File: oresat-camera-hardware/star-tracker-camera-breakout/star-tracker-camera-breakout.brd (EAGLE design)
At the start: 31.8 x 86.4 mm, 7 parts, among them J1 3-1734592-64-1734592-0, J2 3-1734592-64-1734592-0, J7 2X6 FEMALE, J8 2X6 FEMALE

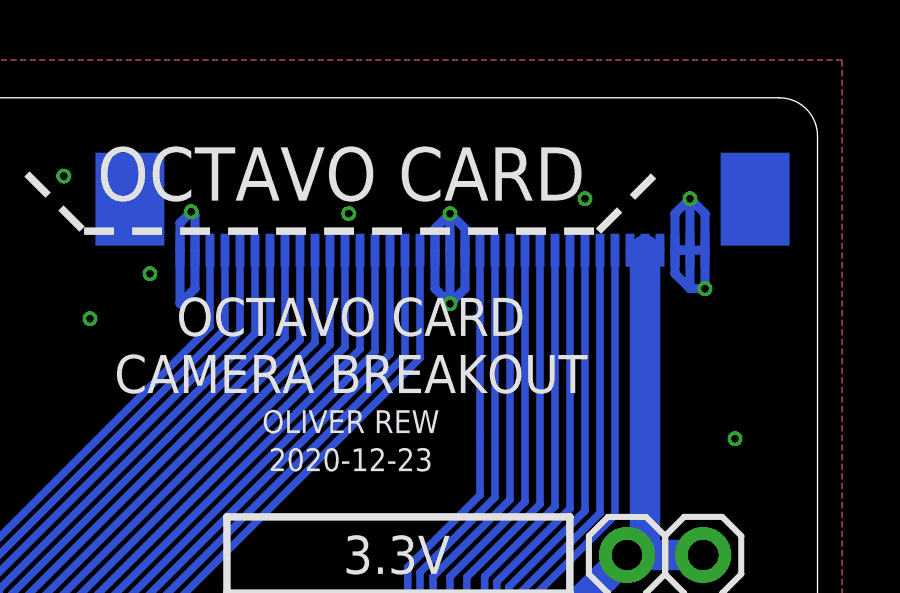
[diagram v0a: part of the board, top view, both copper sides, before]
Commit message: moved a via away from tplace
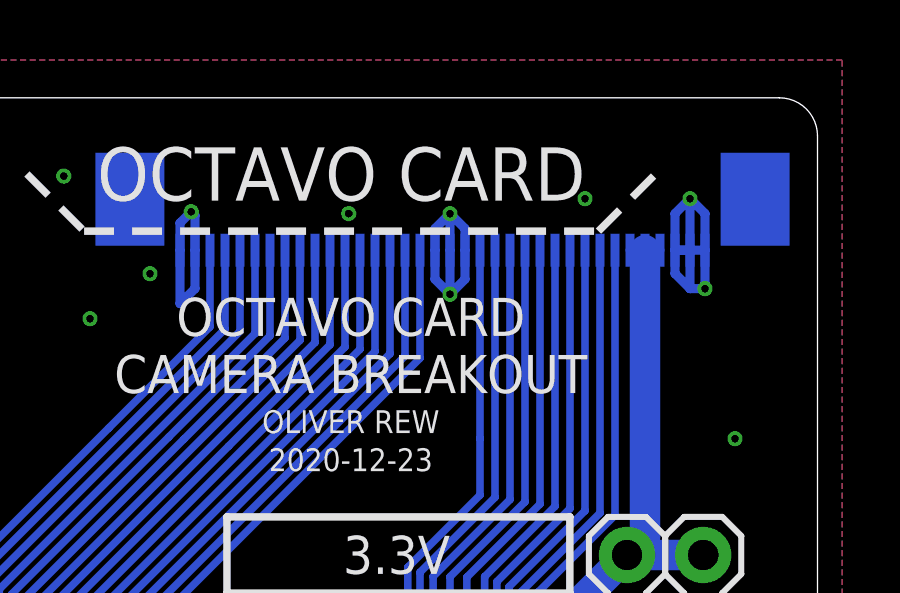
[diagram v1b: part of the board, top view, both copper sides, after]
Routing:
- net GND: track 42.1 -> 41.2 mm
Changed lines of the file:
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@@
 <drawing>
 <settings>
-<setting alwaysvectorfont="yes"/>
+<setting alwaysvectorfont="no"/>
 <setting verticaltext="up"/>
 </settings>
@@
 <via x="15.875" y="3.5" extent="1-16" drill="0.254"/>
 <via x="19.5" y="82.5" extent="1-16" drill="0.254"/>
-<via x="19.5" y="79.5" extent="1-16" drill="0.254"/>
+<via x="19.5" y="79.8125" extent="1-16" drill="0.254"/>
 <wire x1="19" y1="81.28" x2="19" y2="82" width="0.3048" layer="16"/>
 <wire x1="19" y1="82" x2="19.5" y2="82.5" width="0.3048" layer="16"/>
@@
 <wire x1="20" y1="82" x2="19.5" y2="82.5" width="0.3048" layer="16"/>
 <wire x1="19.5" y1="81.28" x2="19.5" y2="82.5" width="0.3048" layer="16"/>
-<wire x1="19" y1="81.28" x2="19" y2="80" width="0.3048" layer="16"/>
-<wire x1="19" y1="80" x2="19.5" y2="79.5" width="0.3048" layer="16"/>
-<wire x1="20" y1="81.28" x2="20" y2="80" width="0.3048" layer="16"/>
-<wire x1="20" y1="80" x2="19.5" y2="79.5" width="0.3048" layer="16"/>
-<wire x1="19.5" y1="81.28" x2="19.5" y2="79.5" width="0.3048" layer="16"/>
+<wire x1="19" y1="81.28" x2="19" y2="80.3125" width="0.3048" layer="16"/>
+<wire x1="19" y1="80.3125" x2="19.5" y2="79.8125" width="0.3048" layer="16"/>
+<wire x1="20" y1="81.28" x2="20" y2="80.3125" width="0.3048" layer="16"/>
+<wire x1="20" y1="80.3125" x2="19.5" y2="79.8125" width="0.3048" layer="16"/>
+<wire x1="19.5" y1="81.28" x2="19.5" y2="79.8125" width="0.3048" layer="16"/>
 <wire x1="27" y1="81.28" x2="27" y2="80.5" width="0.3048" layer="16"/>
 <wire x1="27" y1="80.5" x2="27.5" y2="80" width="0.3048" layer="16"/>
